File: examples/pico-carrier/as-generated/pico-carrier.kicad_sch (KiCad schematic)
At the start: 14 parts, among them J1 5V IN, J3 GP0-GP15, J4 GP16-GP28, PWR, U1 Pico

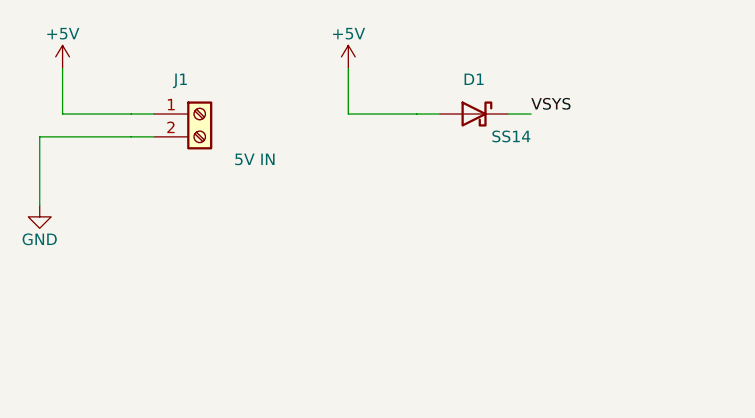
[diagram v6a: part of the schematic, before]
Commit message: feat(examples): round twenty - fuse and clamp every input, state the ESR, damp the clock, control the mute
Redesign of the five worked examples for the items REVIEW.md left open:

- every power input gets a fuse in series and a TVS across the fused rail
  (a resettable fuse on the Pico carrier, whose Schottky already blocks a
  reversed supply); each sheet states what the clamp does not do
- the buck's output capacitor states the ESR the LM2596 loop is designed
  around (SNVS124G 9.1.3), derived from the ripple already on the sheet
- the FPGA's 12 MHz clock leaves its oscillator through 33 ohms
- the DAC's XSMT is driven from the FPGA with a pull-down instead of
  strapped high, so it comes up muted
- the op-amp filter's output goes through a 100 ohm isolation resistor

Generator fixes the round found: _surfaced pruned a via that tapped the
middle of a back-layer spine, and _chamfer_tracks cut the copper out from
under a via sitting a fraction along a leg; both left a net in two pieces
that KiCad's DRC reported. Pin stubs closer than 7.62 mm draw over each
other, so the new parts are spaced for it and the comments say why.

tools/example_images.py renders the README pictures from the regenerated
projects. All five reviewed variants pass their gates and KiCad's DRC on
both matrix versions; the as-generated variants each carry one more
blocking finding (spec.missing_esr). REVIEW.md 25 records the round.

Co-Authored-By: Claude Fable 5.1 <noreply@anthropic.com>
Claude-Session: https://claude.ai/code/session_017JKofiLFxXjzRRnBmFyXuQ
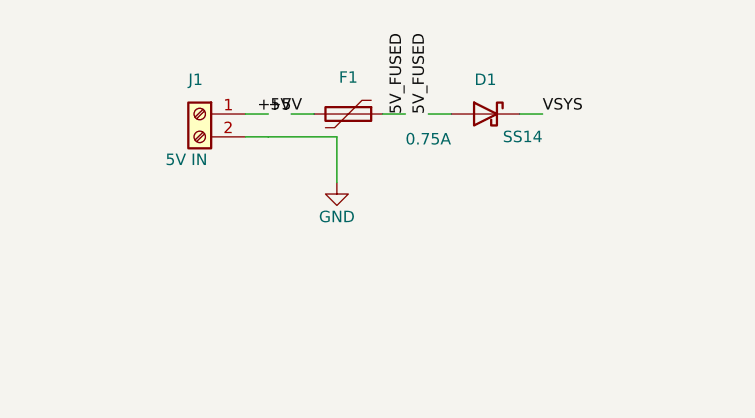
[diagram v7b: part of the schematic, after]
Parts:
- added F1: 0.75A, Fuse:Fuse_1812_4532Metric, symbol Device:Polyfuse
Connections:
- net +5V: now also F1.2; no longer D1.2 (A)
- new net 5V_FUSED: D1.2 (A), F1.1
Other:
- moved on the sheet: D1, J1
